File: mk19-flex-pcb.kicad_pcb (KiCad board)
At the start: 2 copper layers, 269.8 x 46.9 mm, 13 parts

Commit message: adding teardrops, fixing a few odds and ends
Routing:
- net col5: track 609.3 -> 747.1 mm, vias 9 -> 12
- net col3: track 678.9 -> 678.0 mm
- net col4: track 720.7 -> 719.8 mm
- net row0: track 962.0 -> 961.4 mm
- net col0: vias 8 -> 7
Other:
- board size 269.8 x 46.9 mm -> 269.8 x 46.6 mm

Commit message: fixing up the teardrops and spacing out vias for better tolerances
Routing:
- net col5: track 747.1 -> 764.9 mm
- net col4: track 719.8 -> 734.3 mm
- net col3: track 678.0 -> 689.6 mm
- net col0: track 613.3 -> 623.7 mm
- net col1: track 647.5 -> 651.2 mm
- net col2: track 603.3 -> 606.5 mm
- net row0: track 961.4 -> 964.6 mm
- net LED_DOUT_THUMB: track 387.1 -> 384.8 mm
- net row6: track 579.0 -> 577.5 mm
- net row2: track 539.3 -> 540.6 mm
- net GND: track 1465.9 -> 1467.1 mm
- net LED_DIN_THUMB: track 712.4 -> 711.2 mm
- net Net-(ROW0-0-Pin_1): track 156.5 -> 157.4 mm
- net row1: track 539.2 -> 539.8 mm
- net Net-(ROW0-1-Pin_1): track 250.0 -> 249.4 mm
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
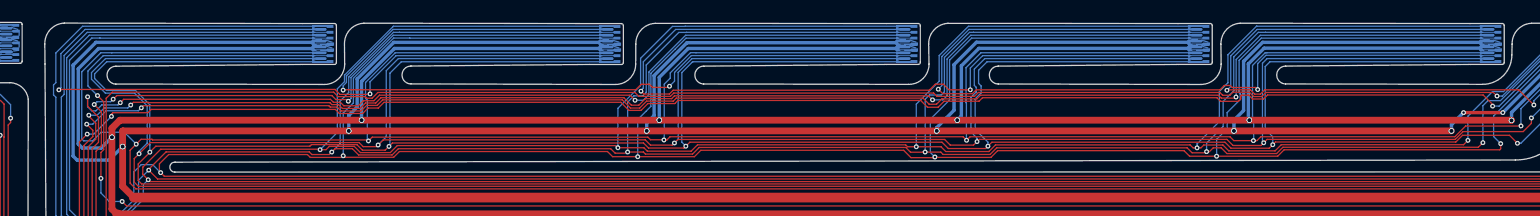
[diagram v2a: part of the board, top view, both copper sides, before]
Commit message: fixing up the tab edge spacing of traces
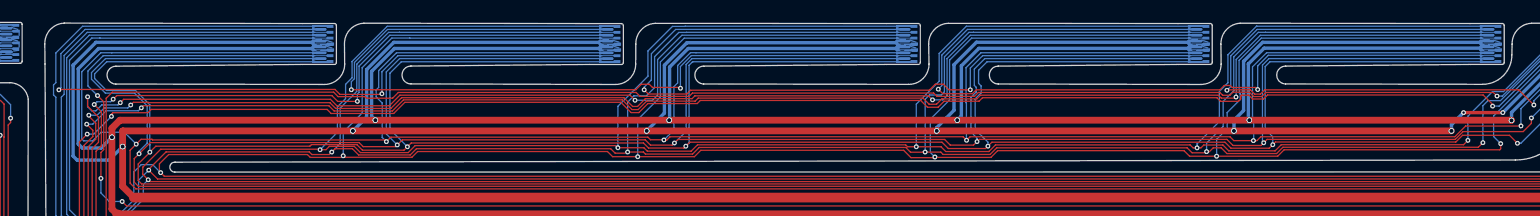
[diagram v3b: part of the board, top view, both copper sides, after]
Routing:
- net col2: track 606.5 -> 607.3 mm
- net col1: track 651.2 -> 652.0 mm
- net +5V: track 1473.2 -> 1472.5 mm
- net Net-(COL-0-Pin_2): track 89.0 -> 89.6 mm
- net Net-(COL-2-Pin_2): track 90.4 -> 89.9 mm
- net row5: track 584.2 -> 584.7 mm

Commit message: final changes before production
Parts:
- added LOGO1: **REF, ct-kicad:awesome-logo, F.Cu at (352.0, 132.8)
- added LOGO2: **REF, ct-kicad:cyboard-logo-10mm, F.Cu at (351.9, 114.8)
- added LOGO3: **REF, ct-kicad:mk19-flex-pcb-qr-12mm, F.Cu at (174.4, 140.0)
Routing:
- net row0: track 964.6 -> 961.8 mm
- net row6: track 577.8 -> 576.6 mm
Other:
- board text added: "COL-0"
- board text added: "COL-1"
- board text added: "COL-2"
- board text added: "COL-3"
- board text added: "COL-4"
- board text added: "COL-5"
- board text added: "MK19-FLEX-PCB-INATOR"
- board text added: "THUMB-0"
- board text added: "THUMB-1"
- board text added: "THUMB-2"
- board text added: "THUMB-3"
- board text added: "THUMB-4"
- board text added: "THUMB-5"
